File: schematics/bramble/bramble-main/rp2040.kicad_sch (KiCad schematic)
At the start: 41 parts, among them IC1 RP2040_QFN56, J2 Conn_01x03, J3 USB_C_Receptacle_USB2.0_16P, J5 U.FL, J7 Conn_02x06_Odd_Even, SW2 BOOT, SW4 RESET, U4 RFM95W-915S2, U6 MT25QL01GBBB8ESF-0SIT, U7 W25Q16JVSS, Y3 Crystal

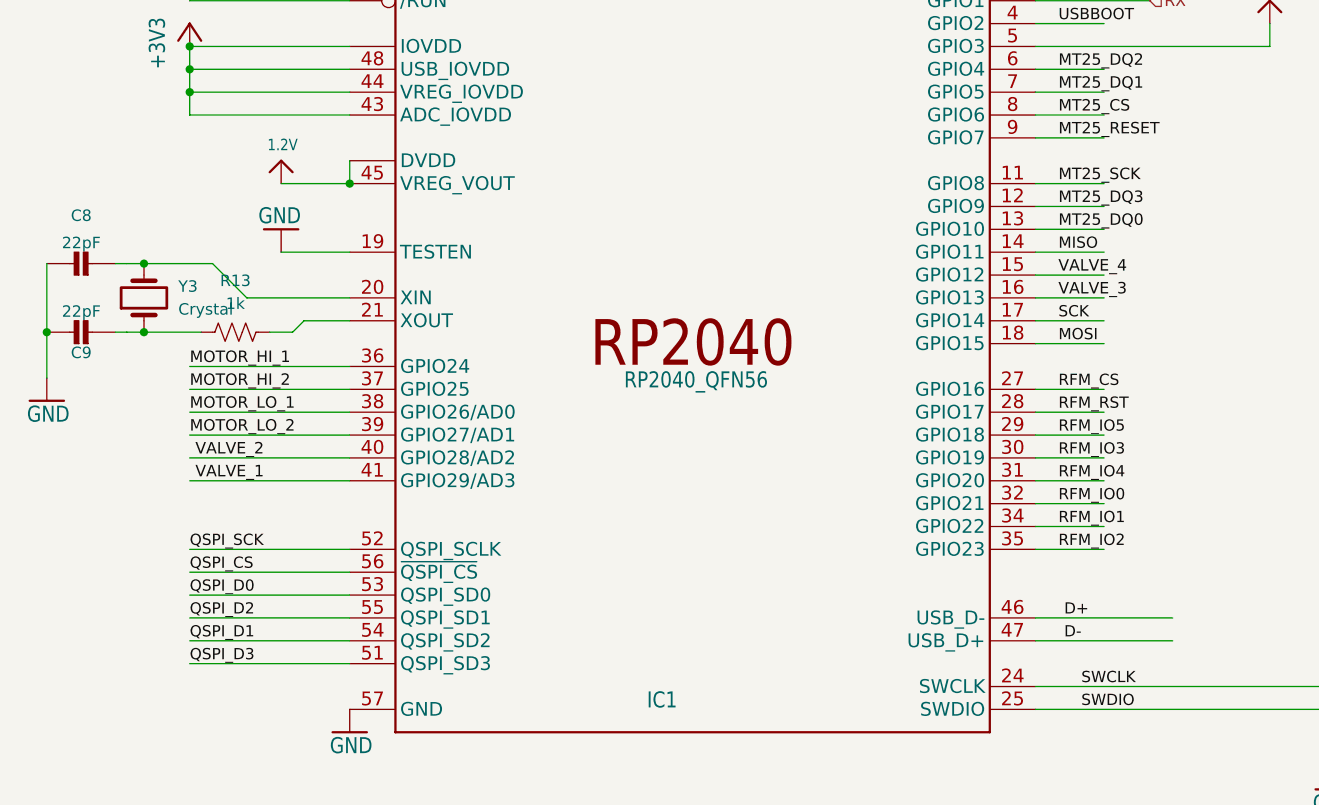
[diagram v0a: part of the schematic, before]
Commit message: fix: swap spi pins, change footprints, etc
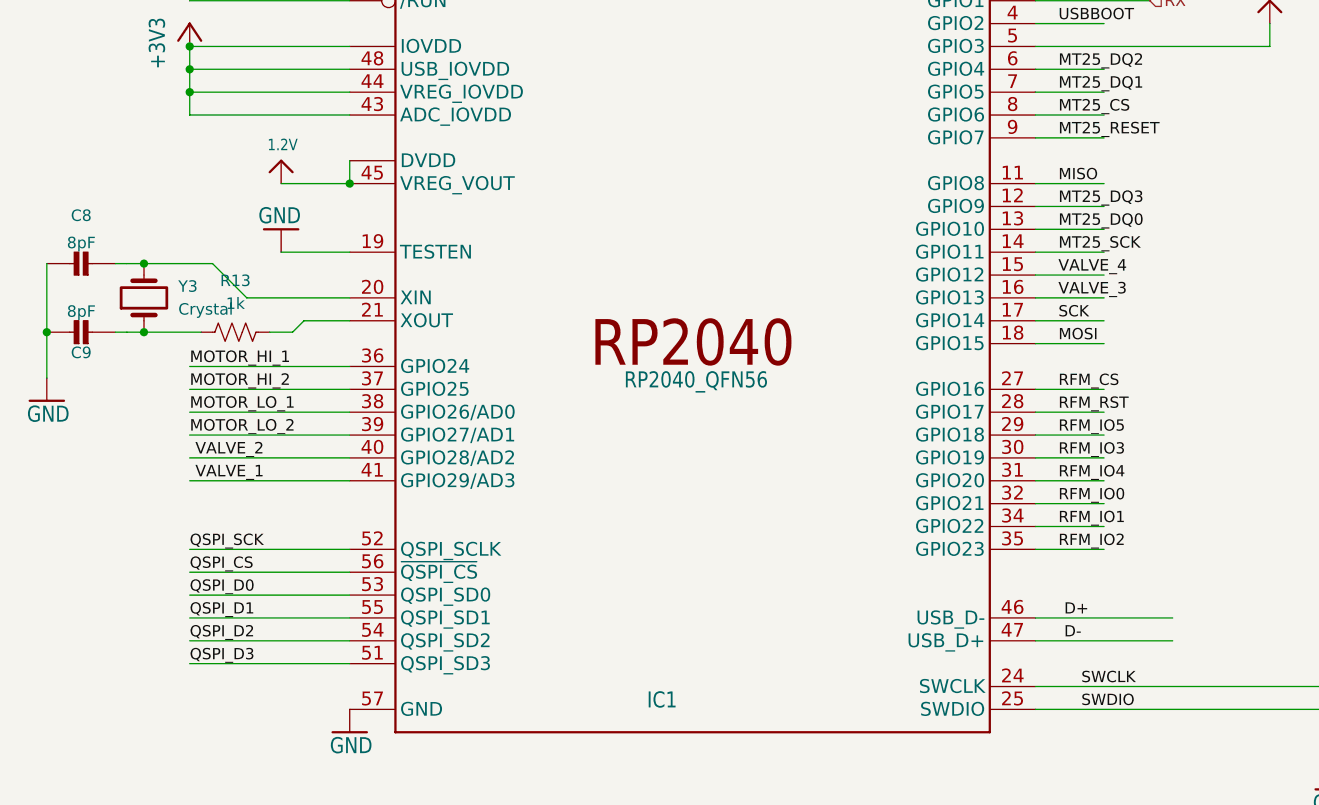
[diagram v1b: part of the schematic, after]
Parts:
- C8, C9: value 22pF -> 8pF
- LED1: footprint LED_SMD:LED_WS2812B_PLCC4_5.0x5.0mm_P3.2mm -> LED_SMD:LED_WS2812B-2020_PLCC4_2.0x2.0mm
- U6: footprint Package_SO:SOP-16_4.55x10.3mm_P1.27mm -> Package_SO:SOIC-16W-12_7.5x10.3mm_P1.27mm
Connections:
- net MISO: now also IC1.11 (GPIO8); no longer IC1.14 (GPIO11)
- net MT25_SCK: now also IC1.14 (GPIO11); no longer IC1.11 (GPIO8)
- net QSPI_D1: now also IC1.55 (QSPI_SD1); no longer IC1.54 (QSPI_SD2)
- net QSPI_D2: now also IC1.54 (QSPI_SD2); no longer IC1.55 (QSPI_SD1)
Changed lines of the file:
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@@
 	(wire
 		(pts
+			(xy 133.35 210.82) (xy 140.97 210.82)
+		)
+		(stroke
+			(width 0.1524)
+			(type solid)
+		)
+	)
+	(wire
+		(pts
 			(xy 49.53 210.82) (xy 57.15 210.82)
 		)
@@
 	(wire
 		(pts
-			(xy 39.37 259.08) (xy 57.15 259.08)
-		)
-		(stroke
-			(width 0.1524)
-			(type solid)
-		)
-	)
-	(wire
-		(pts
 			(xy 195.58 190.5) (xy 210.82 190.5)
 		)
@@
 	(wire
 		(pts
-			(xy 133.35 210.82) (xy 140.97 210.82)
-		)
-		(stroke
-			(width 0.1524)
-			(type solid)
-		)
-	)
-	(wire
-		(pts
 			(xy 226.06 116.84) (xy 226.06 123.19)
 		)
@@
 	(wire
 		(pts
-			(xy 39.37 261.62) (xy 57.15 261.62)
-		)
-		(stroke
-			(width 0.1524)
-			(type solid)
-		)
-	)
-	(wire
-		(pts
 			(xy 133.35 213.36) (xy 140.97 213.36)
 		)
@@
 	(wire
 		(pts
+			(xy 39.37 259.08) (xy 57.15 259.08)
+		)
+		(stroke
+			(width 0.1524)
+			(type solid)
+		)
+	)
+	(wire
+		(pts
 			(xy 384.81 38.1) (xy 394.97 38.1)
 		)
@@
 	(wire
 		(pts
+			(xy 133.35 218.44) (xy 140.97 218.44)
+		)
+		(stroke
+			(width 0.1524)
+			(type solid)
+		)
+	)
+	(wire
+		(pts
 			(xy 326.39 217.805) (xy 326.39 224.155)
 		)
@@
 	(wire
 		(pts
-			(xy 133.35 218.44) (xy 140.97 218.44)
-		)
-		(stroke
-			(width 0.1524)
-			(type solid)
-		)
-	)
-	(wire
-		(pts
 			(xy 114.3 62.23) (xy 114.3 67.31)
 		)
@@
 	(wire
 		(pts
+			(xy 39.37 261.62) (xy 57.15 261.62)
+		)
+		(stroke
+			(width 0.1524)
+			(type solid)
+		)
+	)
+	(wire
+		(pts
 			(xy 259.08 107.95) (xy 275.59 107.95)
 		)
@@
 		)
 	)
+	(label "QSPI_D1"
+		(at 39.37 259.08 0)
+		(effects
+			(font
+				(size 1.2446 1.2446)
+			)
+			(justify left bottom)
+		)
+	)
 	(label "SCK"
 		(at 135.89 226.06 0)
@@
 		)
 	)
-	(label "MT25_SCK"
-		(at 135.89 210.82 0)
-		(effects
-			(font
-				(size 1.27 1.27)
-			)
-			(justify left bottom)
-		)
-	)
 	(label "USBBOOT"
 		(at 114.3 50.8 0)
@@
 		)
 	)
-	(label "MISO"
-		(at 135.89 218.44 0)
-		(effects
-			(font
-				(size 1.2446 1.2446)
-			)
-			(justify left bottom)
-		)
-	)
 	(label "D-"
 		(at 223.52 123.19 0)
@@
 		)
 	)
-	(label "QSPI_D1"
-		(at 39.37 261.62 0)
-		(effects
-			(font
-				(size 1.2446 1.2446)
-			)
-			(justify left bottom)
-		)
-	)
 	(label "RFM_IO4"
 		(at 238.76 198.12 0)
@@
 		)
 	)
+	(label "MT25_SCK"
+		(at 135.89 218.44 0)
+		(effects
+			(font
+				(size 1.27 1.27)
+			)
+			(justify left bottom)
+		)
+	)
 	(label "MT25_CS"
 		(at 316.23 50.8 0)
@@
 		)
 	)
-	(label "QSPI_D2"
-		(at 39.37 259.08 0)
+	(label "MISO"
+		(at 135.89 210.82 0)
 		(effects
 			(font
@@
 		)
 	)
+	(label "QSPI_D2"
+		(at 39.37 261.62 0)
+		(effects
+			(font
+				(size 1.2446 1.2446)
+			)
+			(justify left bottom)
+		)
+	)
 	(label "MOTOR_HI_1"
 		(at 39.37 231.14 0)
@@
 			)
 		)
-		(property "Value" "22pF"
+		(property "Value" "8pF"
 			(at 27.325 217.41 90)
 			(effects
@@
 			)
 		)
-		(property "Footprint" "LED_SMD:LED_WS2812B_PLCC4_5.0x5.0mm_P3.2mm"
+		(property "Footprint" "LED_SMD:LED_WS2812B-2020_PLCC4_2.0x2.0mm"
 			(at 368.3 105.41 0)
 			(effects
@@
 			)
 		)
-		(property "Footprint" "Package_SO:SOP-16_4.55x10.3mm_P1.27mm"
+		(property "Footprint" "Package_SO:SOIC-16W-12_7.5x10.3mm_P1.27mm"
 			(at 328.93 35.56 0)
 			(effects
@@
 			)
 		)
-		(property "Value" "22pF"
+		(property "Value" "8pF"
 			(at 27.325 225.03 90)
 			(effects

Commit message: pre-fab check-in of v2
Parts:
- renumbered C8 to C10, C9 to C11, C10 to C12, C11 to C13, C12 to C14, C13 to C16, C14 to C17, C15 to C18, C16 to C19, C17 to C20, C18 to C21, C19 to C22, C20 to C23, C7 to C9, D3 to D2, J2 to J3, J3 to J4, J7 to J6, R12 to R16, R13 to R17, R14 to R18, R15 to R19, R16 to R20, R17 to R21, R18 to R22, R19 to R23, R20 to R24, R21 to R25, SW4 to SW3, U4 to U5, U7 to U6, U6 to U7, Y3 to Y2
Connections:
- net MISO: now also U7.8 (DQ1)
- net MOSI: now also U7.15 (DQ0)
- net SCK: now also U7.16 (C)
- net ~{RESET}: now also SW3.1
- net D4 renamed RGB_LED
- net RGB_LED: now also IC1.6 (GPIO4)
- net MT25_DQ0: no longer names the net of IC1.13 (GPIO10)
- net MT25_DQ0: no longer U7.15 (DQ0)
- net MT25_DQ1: no longer names the net of IC1.7 (GPIO5)
- net MT25_DQ1: no longer U7.8 (DQ1)
- net MT25_DQ2: no longer names the net of U7.9 (W#/DQ2)
- net MT25_DQ2: no longer IC1.6 (GPIO4)
- net MT25_DQ3: no longer names the net of U7.1 (DQ3/HOLD#)
- net MT25_DQ3: no longer IC1.12 (GPIO9)
- net MT25_SCK: no longer names the net of IC1.14 (GPIO11)
- net MT25_SCK: no longer U7.16 (C)

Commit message: Checking before rollback
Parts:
- renumbered SW2 to BOOT1, C16 to C15, C17 to C16, C18 to C17, C19 to C18, C20 to C19, C21 to C20, C22 to C21, C23 to C22, D2 to D1, J4 to J1, J5 to J2, J6 to J3, SW3 to RESET1, J3 to RPI_DEBUG1, LED1 to RPI_STATUS1, U5 to U4, U6 to U5, U7 to U6
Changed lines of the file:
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@@
 		(dnp no)
 		(fields_autoplaced yes)
-		(property "Reference" "SW3"
+		(property "Reference" "RESET1"
 			(at 135.89 58.4199 90)
 			(effects
@@
 			(project ""
 				(path "/e35d7dcf-51bd-456f-89cf-e52d660079b4/74ee86d6-15f8-4467-9b29-c5ab14125d21"
-					(reference "SW3")
+					(reference "RESET1")
 					(unit 1)
 				)
@@
 		(dnp no)
 		(fields_autoplaced yes)
-		(property "Reference" "J6"
+		(property "Reference" "J3"
 			(at 316.23 199.39 0)
 			(effects
@@
 			(project ""
 				(path "/e35d7dcf-51bd-456f-89cf-e52d660079b4/74ee86d6-15f8-4467-9b29-c5ab14125d21"
-					(reference "J6")
+					(reference "J3")
 					(unit 1)
 				)
@@
 		(dnp no)
 		(fields_autoplaced yes)
-		(property "Reference" "J5"
+		(property "Reference" "J2"
 			(at 269.24 189.5231 0)
 			(effects
@@
 			(project ""
 				(path "/e35d7dcf-51bd-456f-89cf-e52d660079b4/74ee86d6-15f8-4467-9b29-c5ab14125d21"
-					(reference "J5")
+					(reference "J2")
 					(unit 1)
 				)
@@
 		(on_board yes)
 		(dnp no)
-		(property "Reference" "LED1"
+		(property "Reference" "RPI_STATUS1"
 			(at 368.3 105.41 0)
 			(effects
@@
 			(project "bramble"
 				(path "/e35d7dcf-51bd-456f-89cf-e52d660079b4/74ee86d6-15f8-4467-9b29-c5ab14125d21"
-					(reference "LED1")
+					(reference "RPI_STATUS1")
 					(unit 1)
 				)
@@
 		(on_board yes)
 		(dnp no)
-		(property "Reference" "C16"
+		(property "Reference" "C15"
 			(at 56.13 96.54 90)
 			(effects
@@
 			(project "bramble"
 				(path "/e35d7dcf-51bd-456f-89cf-e52d660079b4/74ee86d6-15f8-4467-9b29-c5ab14125d21"
-					(reference "C16")
+					(reference "C15")
 					(unit 1)
 				)
@@
 		(dnp no)
 		(fields_autoplaced yes)
-		(property "Reference" "J3"
+		(property "Reference" "RPI_DEBUG1"
 			(at 177.8 267.9699 0)
 			(effects
@@
 			(project ""
 				(path "/e35d7dcf-51bd-456f-89cf-e52d660079b4/74ee86d6-15f8-4467-9b29-c5ab14125d21"
-					(reference "J3")
+					(reference "RPI_DEBUG1")
 					(unit 1)
 				)
@@
 		(dnp no)
 		(fields_autoplaced yes)
-		(property "Reference" "D2"
+		(property "Reference" "D1"
 			(at 116.84 43.1799 90)
 			(effects
@@
 			(project ""
 				(path "/e35d7dcf-51bd-456f-89cf-e52d660079b4/74ee86d6-15f8-4467-9b29-c5ab14125d21"
-					(reference "D2")
+					(reference "D1")
 					(unit 1)
 				)
@@
 		(on_board yes)
 		(dnp no)
-		(property "Reference" "C21"
+		(property "Reference" "C20"
 			(at 96.77 96.54 90)
 			(effects
@@
 			(project "bramble"
 				(path "/e35d7dcf-51bd-456f-89cf-e52d660079b4/74ee86d6-15f8-4467-9b29-c5ab14125d21"
-					(reference "C21")
+					(reference "C20")
 					(unit 1)
 				)
@@
 		(on_board yes)
 		(dnp no)
-		(property "Reference" "C23"
+		(property "Reference" "C22"
 			(at 112.01 96.54 90)
 			(effects
@@
 			(project "bramble"
 				(path "/e35d7dcf-51bd-456f-89cf-e52d660079b4/74ee86d6-15f8-4467-9b29-c5ab14125d21"
-					(reference "C23")
+					(reference "C22")
 					(unit 1)
 				)
@@
 		(dnp no)
 		(fields_autoplaced yes)
-		(property "Reference" "U5"
+		(property "Reference" "U4"
 			(at 225.6633 182.88 0)
 			(effects
@@
 			(project ""
 				(path "/e35d7dcf-51bd-456f-89cf-e52d660079b4/74ee86d6-15f8-4467-9b29-c5ab14125d21"
-					(reference "U5")
+					(reference "U4")
 					(unit 1)
 				)
@@
 		(dnp no)
 		(fields_autoplaced yes)
-		(property "Reference" "U6"
+		(property "Reference" "U5"
 			(at 297.18 101.5999 0)
 			(effects
@@
 			(project ""
 				(path "/e35d7dcf-51bd-456f-89cf-e52d660079b4/74ee86d6-15f8-4467-9b29-c5ab14125d21"
-					(reference "U6")
+					(reference "U5")
 					(unit 1)
 				)
@@
 		(dnp no)
 		(fields_autoplaced yes)
-		(property "Reference" "SW2"
+		(property "Reference" "BOOT1"
 			(at 118.11 55.8799 90)
 			(effects
@@
 			(project "bramble"
 				(path "/e35d7dcf-51bd-456f-89cf-e52d660079b4/74ee86d6-15f8-4467-9b29-c5ab14125d21"
-					(reference "SW2")
+					(reference "BOOT1")
 					(unit 1)
 				)
@@
 		(on_board yes)
 		(dnp no)
-		(property "Reference" "C18"
+		(property "Reference" "C17"
 			(at 73.91 96.54 90)
 			(effects
@@
 			(project "bramble"
 				(path "/e35d7dcf-51bd-456f-89cf-e52d660079b4/74ee86d6-15f8-4467-9b29-c5ab14125d21"
-					(reference "C18")
+					(reference "C17")
 					(unit 1)
 				)
@@
 		(dnp no)
 		(fields_autoplaced yes)
-		(property "Reference" "J4"
+		(property "Reference" "J1"
 			(at 198.12 77.47 0)
 			(effects
@@
 			(project ""
 				(path "/e35d7dcf-51bd-456f-89cf-e52d660079b4/74ee86d6-15f8-4467-9b29-c5ab14125d21"
-					(reference "J4")
+					(reference "J1")
 					(unit 1)
 				)
@@
 		(on_board yes)
 		(dnp no)
-		(property "Reference" "C22"
+		(property "Reference" "C21"
 			(at 104.39 96.54 90)
 			(effects
@@
 			(project "bramble"
 				(path "/e35d7dcf-51bd-456f-89cf-e52d660079b4/74ee86d6-15f8-4467-9b29-c5ab14125d21"
-					(reference "C22")
+					(reference "C21")
 					(unit 1)
 				)
@@
 		(on_board yes)
 		(dnp no)
-		(property "Reference" "C20"
+		(property "Reference" "C19"
 			(at 89.15 96.54 90)
 			(effects
@@
 			(project "bramble"
 				(path "/e35d7dcf-51bd-456f-89cf-e52d660079b4/74ee86d6-15f8-4467-9b29-c5ab14125d21"
-					(reference "C20")
+					(reference "C19")
 					(unit 1)
 				)
@@
 		(dnp no)
 		(fields_autoplaced yes)
-		(property "Reference" "U7"
+		(property "Reference" "U6"
 			(at 356.87 25.4 0)
 			(effects
@@
 			(project ""
 				(path "/e35d7dcf-51bd-456f-89cf-e52d660079b4/74ee86d6-15f8-4467-9b29-c5ab14125d21"
-					(reference "U7")
+					(reference "U6")
 					(unit 1)
 				)
@@
 		(on_board yes)
 		(dnp no)
-		(property "Reference" "C17"
+		(property "Reference" "C16"
 			(at 66.29 96.54 90)
 			(effects
@@
 			(project "bramble"
 				(path "/e35d7dcf-51bd-456f-89cf-e52d660079b4/74ee86d6-15f8-4467-9b29-c5ab14125d21"
-					(reference "C17")
+					(reference "C16")
 					(unit 1)
 				)
@@
 		(on_board yes)
 		(dnp no)
-		(property "Reference" "C19"
+		(property "Reference" "C18"
 			(at 81.53 96.54 90)
 			(effects
@@
 			(project "bramble"
 				(path "/e35d7dcf-51bd-456f-89cf-e52d660079b4/74ee86d6-15f8-4467-9b29-c5ab14125d21"
-					(reference "C19")
+					(reference "C18")
 					(unit 1)
 				)

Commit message: Check in some of the v3 change
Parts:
- removed RPI_STATUS1: WS2812B_SK6805_1515, LED_SMD:LED_WS2812B-2020_PLCC4_2.0x2.0mm, symbol Adafruit Feather RP2040 RFM-eagle-import:WS2812B_SK6805_1515
- added RPI_STATUS1: WS2812B-2020, LED_SMD:LED_WS2812B-2020_PLCC4_2.0x2.0mm, symbol LED:WS2812B-2020
- SW3: renamed from RESET1; Silkscreen_Label (none) -> RESET
- renumbered D1 to D2, RPI_DEBUG1 to J3, J1 to J4, J2 to J5, J3 to J6, BOOT1 to SW2
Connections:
- net +3V3: now also RPI_STATUS1.4 (VDD)
- net GND: now also RPI_STATUS1.2 (VSS)
- net RGB_LED: now also RPI_STATUS1.3 (DIN)
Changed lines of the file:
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@@
 	(wire
 		(pts
+			(xy 361.442 104.14) (xy 365.76 104.14)
+		)
+		(stroke
+			(width 0)
+			(type default)
+		)
+	)
+	(wire
+		(pts
 			(xy 23.495 219.71) (xy 23.495 227.33)
 		)
@@
 	(wire
 		(pts
-			(xy 373.38 90.17) (xy 373.38 87.63)
+			(xy 373.38 87.63) (xy 373.38 96.52)
 		)
 		(stroke
@@
 	(wire
 		(pts
-			(xy 355.6 107.95) (xy 345.44 107.95)
+			(xy 361.442 104.14) (xy 351.282 104.14)
 		)
 		(stroke
@@
 	(wire
 		(pts
+			(xy 373.38 111.76) (xy 373.38 116.586)
+		)
+		(stroke
+			(width 0)
+			(type default)
+		)
+	)
+	(wire
+		(pts
 			(xy 57.15 236.22) (xy 39.37 236.22)
 		)
@@
 	)
 	(label "RGB_LED"
-		(at 345.44 107.95 0)
+		(at 351.282 104.14 0)
 		(effects
 			(font
@@
 		(dnp no)
 		(fields_autoplaced yes)
-		(property "Reference" "RESET1"
+		(property "Reference" "SW3"
 			(at 135.89 58.4199 90)
 			(effects
@@
 				)
 				(justify left)
+				(hide yes)
 			)
 		)
@@
 			)
 		)
+		(property "Silkscreen_Label" "RESET"
+			(at 132.08 59.69 90)
+			(effects
+				(font
+					(size 1.27 1.27)
+				)
+				(hide yes)
+			)
+		)
 		(pin "2"
 		)
@@
 			(project ""
 				(path "/e35d7dcf-51bd-456f-89cf-e52d660079b4/74ee86d6-15f8-4467-9b29-c5ab14125d21"
-					(reference "RESET1")
+					(reference "SW3")
 					(unit 1)
 				)
@@
 		(dnp no)
 		(fields_autoplaced yes)
-		(property "Reference" "J3"
+		(property "Reference" "J6"
 			(at 316.23 199.39 0)
 			(effects
@@
 			(project ""
 				(path "/e35d7dcf-51bd-456f-89cf-e52d660079b4/74ee86d6-15f8-4467-9b29-c5ab14125d21"
-					(reference "J3")
+					(reference "J6")
 					(unit 1)
 				)
@@
 		(dnp no)
 		(fields_autoplaced yes)
-		(property "Reference" "J2"
+		(property "Reference" "J5"
 			(at 269.24 189.5231 0)
 			(effects
@@
 			(project ""
 				(path "/e35d7dcf-51bd-456f-89cf-e52d660079b4/74ee86d6-15f8-4467-9b29-c5ab14125d21"
-					(reference "J2")
-					(unit 1)
-				)
-			)
-		)
-	)
-	(symbol
-		(lib_id "Adafruit Feather RP2040 RFM-eagle-import:WS2812B_SK6805_1515")
-		(at 368.3 105.41 0)
-		(unit 1)
-		(exclude_from_sim no)
-		(in_bom yes)
-		(on_board yes)
-		(dnp no)
-		(property "Reference" "RPI_STATUS1"
-			(at 368.3 105.41 0)
-			(effects
-				(font
-					(size 1.27 1.27)
-				)
-				(hide yes)
-			)
-		)
-		(property "Value" "WS2812B_SK6805_1515"
-			(at 368.3 105.41 0)
-			(effects
-				(font
-					(size 1.27 1.27)
-				)
-				(hide yes)
-			)
-		)
-		(property "Footprint" "LED_SMD:LED_WS2812B-2020_PLCC4_2.0x2.0mm"
-			(at 368.3 105.41 0)
-			(effects
-				(font
-					(size 1.27 1.27)
-				)
-				(hide yes)
-			)
-		)
-		(property "Datasheet" ""
-			(at 368.3 105.41 0)
-			(effects
-				(font
-					(size 1.27 1.27)
-				)
-				(hide yes)
-			)
-		)
-		(property "Description" ""
-			(at 368.3 105.41 0)
-			(effects
-				(font
-					(size 1.27 1.27)
-				)
-				(hide yes)
-			)
-		)
-		(pin "1"
-		)
-		(pin "4"
-		)
-		(pin "2"
-		)
-		(pin "3"
-		)
-		(instances
-			(project "bramble"
-				(path "/e35d7dcf-51bd-456f-89cf-e52d660079b4/74ee86d6-15f8-4467-9b29-c5ab14125d21"
-					(reference "RPI_STATUS1")
+					(reference "J5")
 					(unit 1)
 				)
@@
 		(dnp no)
 		(fields_autoplaced yes)
-		(property "Reference" "RPI_DEBUG1"
+		(property "Reference" "J3"
 			(at 177.8 267.9699 0)
 			(effects
@@
 			(project ""
 				(path "/e35d7dcf-51bd-456f-89cf-e52d660079b4/74ee86d6-15f8-4467-9b29-c5ab14125d21"
-					(reference "RPI_DEBUG1")
+					(reference "J3")
 					(unit 1)
 				)
@@
 		(dnp no)
 		(fields_autoplaced yes)
-		(property "Reference" "D1"
+		(property "Reference" "D2"
 			(at 116.84 43.1799 90)
 			(effects
@@
 			(project ""
 				(path "/e35d7dcf-51bd-456f-89cf-e52d660079b4/74ee86d6-15f8-4467-9b29-c5ab14125d21"
-					(reference "D1")
+					(reference "D2")
+					(unit 1)
+				)
+			)
+		)
+	)
+	(symbol
+		(lib_id "LED:WS2812B-2020")
+		(at 373.38 104.14 0)
+		(unit 1)
+		(exclude_from_sim no)
+		(in_bom yes)
+		(on_board yes)
+		(dnp no)
+		(fields_autoplaced yes)
+		(property "Reference" "RPI_STATUS1"
+			(at 387.35 97.7198 0)
+			(effects
+				(font
+					(size 1.27 1.27)
+				)
+			)
+		)
+		(property "Value" "WS2812B-2020"
+			(at 387.35 100.2598 0)
+			(effects
+				(font
+					(size 1.27 1.27)
+				)
+			)
+		)
+		(property "Footprint" "LED_SMD:LED_WS2812B-2020_PLCC4_2.0x2.0mm"
+			(at 374.65 111.76 0)
+			(effects
+				(font
+					(size 1.27 1.27)
+				)
+				(justify left top)
+				(hide yes)
+			)
+		)
+		(property "Datasheet" "https://cdn-shop.adafruit.com/product-files/4684/4684_WS2812B-2020_V1.3_EN.pdf"
+			(at 375.92 113.665 0)
+			(effects
+				(font
+					(size 1.27 1.27)
+				)
+				(justify left top)
+				(hide yes)
+			)
+		)
+		(property "Description" "RGB LED with integrated controller, 2.0 x 2.0 mm, 12 mA"
+			(at 373.38 104.14 0)
+			(effects
+				(font
+					(size 1.27 1.27)
+				)
+				(hide yes)
+			)
+		)
+		(pin "2"
+		)
+		(pin "4"
+		)
+		(pin "3"
+		)
+		(pin "1"
+		)
+		(instances
+			(project ""
+				(path "/e35d7dcf-51bd-456f-89cf-e52d660079b4/74ee86d6-15f8-4467-9b29-c5ab14125d21"
+					(reference "RPI_STATUS1")
 					(unit 1)
 				)
@@
 	(symbol
 		(lib_id "Adafruit Feather RP2040 RFM-eagle-import:supply1_371_GND")
-		(at 368.3 118.11 0)
+		(at 373.38 119.126 0)
 		(unit 1)
 		(exclude_from_sim no)
@@
 		(dnp no)
 		(property "Reference" "#GND011"
-			(at 368.3 118.11 0)
+			(at 373.38 119.126 0)
 			(effects
 				(font
@@
 		)
 		(property "Value" "GND"
-			(at 365.76 120.65 0)
+			(at 370.84 121.666 0)
 			(effects
 				(font
@@
 		)
 		(property "Footprint" ""
-			(at 368.3 118.11 0)
+			(at 373.38 119.126 0)
 			(effects
 				(font
@@
 		)
 		(property "Datasheet" ""
-			(at 368.3 118.11 0)
+			(at 373.38 119.126 0)
 			(effects
 				(font
@@
 		)
 		(property "Description" ""
-			(at 368.3 118.11 0)
+			(at 373.38 119.126 0)
 			(effects
 				(font
@@
 		(dnp no)
 		(fields_autoplaced yes)
-		(property "Reference" "BOOT1"
+		(property "Reference" "SW2"
 			(at 118.11 55.8799 90)
 			(effects
@@
 				)
 				(justify left)
+				(hide yes)
 			)
 		)
@@
 			(project "bramble"
 				(path "/e35d7dcf-51bd-456f-89cf-e52d660079b4/74ee86d6-15f8-4467-9b29-c5ab14125d21"
-					(reference "BOOT1")
+					(reference "SW2")
 					(unit 1)
 				)
@@
 		(dnp no)
 		(fields_autoplaced yes)
-		(property "Reference" "J1"
+		(property "Reference" "J4"
 			(at 198.12 77.47 0)
 			(effects
@@
 			(project ""
 				(path "/e35d7dcf-51bd-456f-89cf-e52d660079b4/74ee86d6-15f8-4467-9b29-c5ab14125d21"
-					(reference "J1")
+					(reference "J4")
 					(unit 1)
 				)
